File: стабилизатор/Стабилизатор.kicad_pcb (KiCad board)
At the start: 2 copper layers, 35 parts, among them J1 V_IN, J2 +43V, J3 -43V, J4 +11V, J5 -11V, J6 +31V, J7 -31V, J8 V_OUT, Q1 BD140, Q2 BD139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

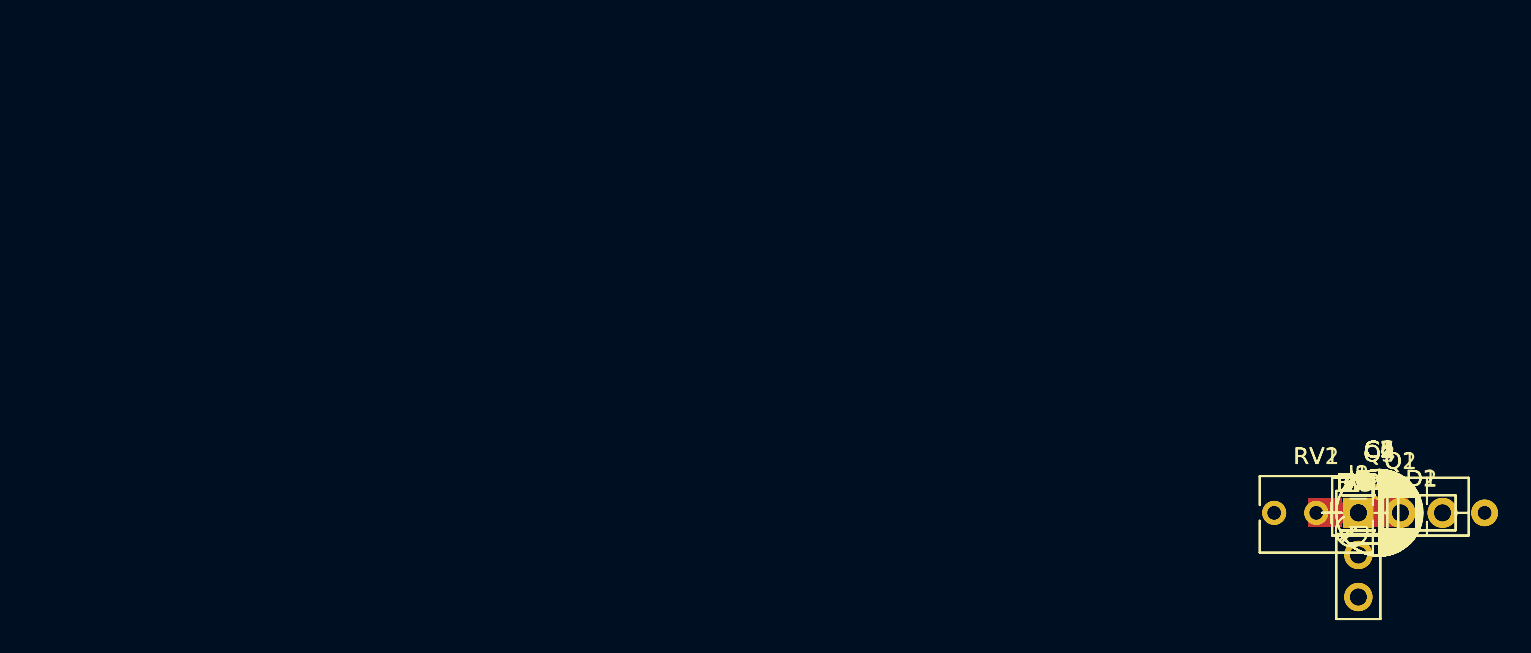
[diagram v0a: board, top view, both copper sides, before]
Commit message: Разводка платы стабилизатора
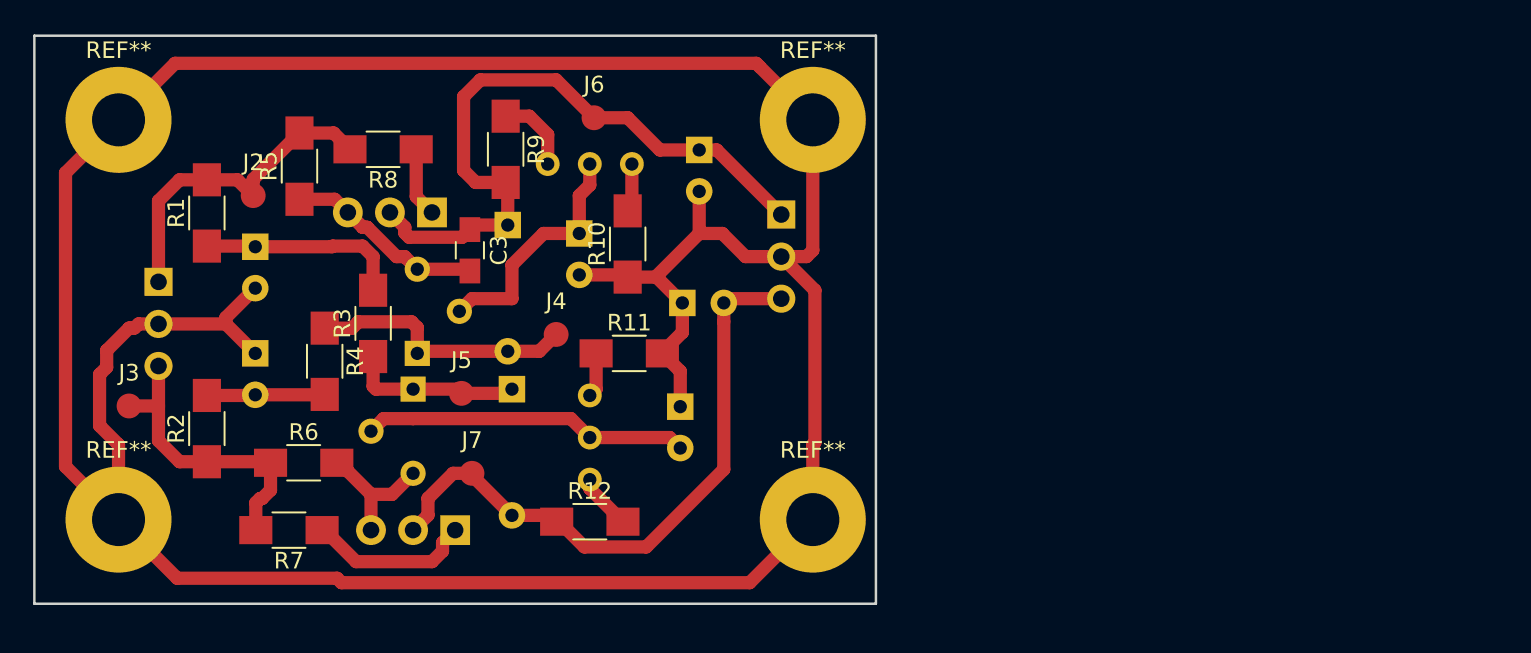
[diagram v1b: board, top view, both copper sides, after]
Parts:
- added REF**: MountingHole_3.2mm_M3_Pad, Mounting_Holes:MountingHole_3.2mm_M3_Pad, F.Cu at (115.6, 105.4)
- added REF**: MountingHole_3.2mm_M3_Pad, Mounting_Holes:MountingHole_3.2mm_M3_Pad, F.Cu at (73.7, 105.4)
- added REF**: MountingHole_3.2mm_M3_Pad, Mounting_Holes:MountingHole_3.2mm_M3_Pad, F.Cu at (115.6, 81.3)
- added REF**: MountingHole_3.2mm_M3_Pad, Mounting_Holes:MountingHole_3.2mm_M3_Pad, F.Cu at (73.7, 81.3)
- C1, C2, C4, C5, C6, C7, D1, D2, J1, J8, Q1, Q2, RV1, RV2: moved to B.Cu
- Q3, Q4: footprint TO_SOT_Packages_THT:TO-92_Molded_Narrow -> TO_SOT_Packages_THT:TO-92_Molded_Wide; moved to B.Cu
- moved J3 74.5 mm to (74.3, 98.6)
- moved J1 73.8 mm to (76.1, 91.1), turned to 180 degrees
- moved R1 71.8 mm to (79.0, 86.9), turned to 90 degrees
- moved R2 69.7 mm to (79.0, 99.9), turned to 90 degrees
- moved J2 69.4 mm to (81.8, 85.9)
- moved C1 68.5 mm to (81.9, 88.9), turned to 270 degrees
- moved C2 67.3 mm to (81.9, 95.4), turned to 270 degrees
- moved R5 67.3 mm to (84.6, 84.1), turned to 90 degrees
- moved R7 64.6 mm to (83.9, 106.0), turned to 180 degrees
- moved R6 63.7 mm to (84.8, 102.0)
- moved R4 63.1 mm to (86.1, 95.9), turned to 270 degrees
- moved R8 62.8 mm to (89.6, 83.1), turned to 180 degrees
- moved R3 60.6 mm to (89.0, 93.6), turned to 90 degrees
- moved Q1 58.8 mm to (92.6, 86.9), turned to 180 degrees
- moved Q3 57.6 mm to (91.7, 95.4), turned to 90 degrees
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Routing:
- net Net-(C1-Pad2): track 0.00 -> 196.2 mm
- net Net-(C3-Pad1): track 0.00 -> 41.1 mm
- net Net-(C7-Pad2): track 0.00 -> 38.3 mm
- net Net-(J1-Pad1): track 0.00 -> 19.9 mm
- net Net-(C5-Pad2): track 0.00 -> 19.7 mm
- net Net-(J1-Pad3): track 0.00 -> 18.1 mm
- net Net-(D2-Pad2): track 0.00 -> 16.3 mm
- net Net-(C4-Pad1): track 0.00 -> 14.8 mm
- net Net-(C1-Pad1): track 0.00 -> 12.4 mm
- net Net-(C3-Pad2): track 0.00 -> 12.4 mm
- net Net-(D1-Pad1): track 0.00 -> 10.5 mm
- net Net-(Q2-Pad1): track 0.00 -> 9.91 mm
- net Net-(Q2-Pad3): track 0.00 -> 8.08 mm
- net Net-(C2-Pad2): track 0.00 -> 7.14 mm
- net Net-(R9-Pad1): track 0.00 -> 4.78 mm
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- added copper zone on F.Cu, net Net-(C1-Pad2)
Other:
- board outline added: 50.8 x 34.3 mm
